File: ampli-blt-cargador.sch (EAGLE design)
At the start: 9 parts, among them IC1 TP4056

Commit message: correción de archivos
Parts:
- added BAT+, BAT+1, BAT-, BAT-1: LSP10, solpad:LSP10
- added C10, C7, C8, C9: 10uf, rcl:C-USC1206
- added C3, C4, C5, C6: (no value), rcl:C-EUC1206
- added IC2: TP4056, TP4056:TP4056
- added J1, J2, J3, J4: B2B-XH-A(LF)(SN), B2B-XH-A_LF__SN_:B2B-XH-A(LF)(SN)
- added J5, J6: UJC-HP-3-SMT-TR, UJC-HP-3-SMT-TR:UJC-HP-3-SMT-TR
- added LED3, LED4: (no value), led:LEDSML1206
- added R10, R11, R6, R7: 1k, rcl:R-US_R1206
- added R12, R8: 1k2, rcl:R-US_R1206
- added R5, R9: 0.4, rcl:R-US_R1206
- added U1: LM4950TSX/NOPB, LM4950TSX_NOPB:LM4950TSX/NOPB
- added XA1: B3P-VH(LF)(SN), B3P-VH_LF__SN_:B3P-VH(LF)(SN)
- C1, C2: device rcl:C-USC1206 -> rcl:C-EUC1206
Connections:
- new net N$10: C5.1, J2.2
- new net N$11: C2.2, J4.2
- new net N$13: C7.1, IC1.CE, IC1.VCC, LED1.A, LED2.A, R5.2
- new net N$14: LED1.C, R6.1
- new net N$15: IC1.CHRG, R6.2
- new net N$16: LED2.C, R7.1
- new net N$17: IC1.STDBY, R7.2
- new net N$18: IC1.PROG, R8.1
- new net N$19: C9.1, IC2.CE, IC2.VCC, LED3.A, LED4.A, R9.2
- new net N$20: LED3.C, R10.1
- new net N$21: IC2.CHRG, R10.2
- new net N$22: LED4.C, R11.1
- new net N$23: IC2.STDBY, R11.2
- new net N$24: IC2.PROG, R12.1
- new net N$7: C4.2, R4.2, U1.VOUTA
- new net N$8: C5.2, R3.2, U1.VOUTB
- new net N$9: C1.2, J3.2
- net GND: now also BAT-.MP, BAT-1.MP, C10.2, C3.2, C6.2, C7.2, C8.2, C9.2, IC2.GND, IC2.TEMP, J1.1, J2.1, J3.1, J4.1, J5.GND, J6.GND, R12.2, R8.2, U1.GND, U1.GND(TAB), U1.GND_2, XA1.1; no longer C1.2, C2.2, R4.2
- net N$1: now also R2.2, R3.1, U1.VINB; no longer C1.1, IC1.CE, IC1.VCC, LED1.A, LED2.A, R1.2
- net N$2: now also C2.1, R2.1; no longer IC1.PROG, R4.1
- net N$3: now also R1.2, R4.1, U1.VINA; no longer LED1.C, R2.1
- net N$4: now also C1.1, R1.1; no longer IC1.CHRG, R2.2
- net N$5: now also C6.1, U1.BYPASS; no longer LED2.C, R3.1
- net N$6: now also C4.1, J1.2; no longer IC1.STDBY, R3.2
- net VCC: now also J5.V-BUS, J6.V-BUS, R5.1, R9.1; no longer R1.1
- net VDD: now also BAT+.MP, BAT+1.MP, C10.1, C3.1, C8.1, IC2.BAT, U1.VDD, XA1.2, XA1.3; no longer C2.1
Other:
- note added: "amplificador"
- note added: "cargador"

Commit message: se termino el area de carga de pila, falta agregar el area de bluetooth
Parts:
- added C11: (no value), rcl:C-EUC1206
- added C12: 10uf, rcl:C-USC1206
- added IC3: DW01A, DW01A:DW01A
- added J7: B2B-XH-A(LF)(SN), B2B-XH-A_LF__SN_:B2B-XH-A(LF)(SN)
- added Q1: FS8205A, FS8205A:FS8205A
- added R13: 1k, rcl:R-US_R1206
- added R14: 100, rcl:R-US_R1206
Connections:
- new net B+: C10.1, C12.1, IC2.BAT, J7.2, R14.2
- new net B-: C10.2, C11.2, C12.2, IC3.GND, J7.1, Q1.S2
- new net N$12: IC3.CS, R13.1
- new net N$25: IC3.OC, Q1.G2
- new net N$26: IC3.OD, Q1.G1
- new net N$27: C11.1, IC3.VCC, R14.1
- net GND: now also Q1.S1, R13.2; no longer C10.2
- net VDD: no longer C10.1, IC2.BAT

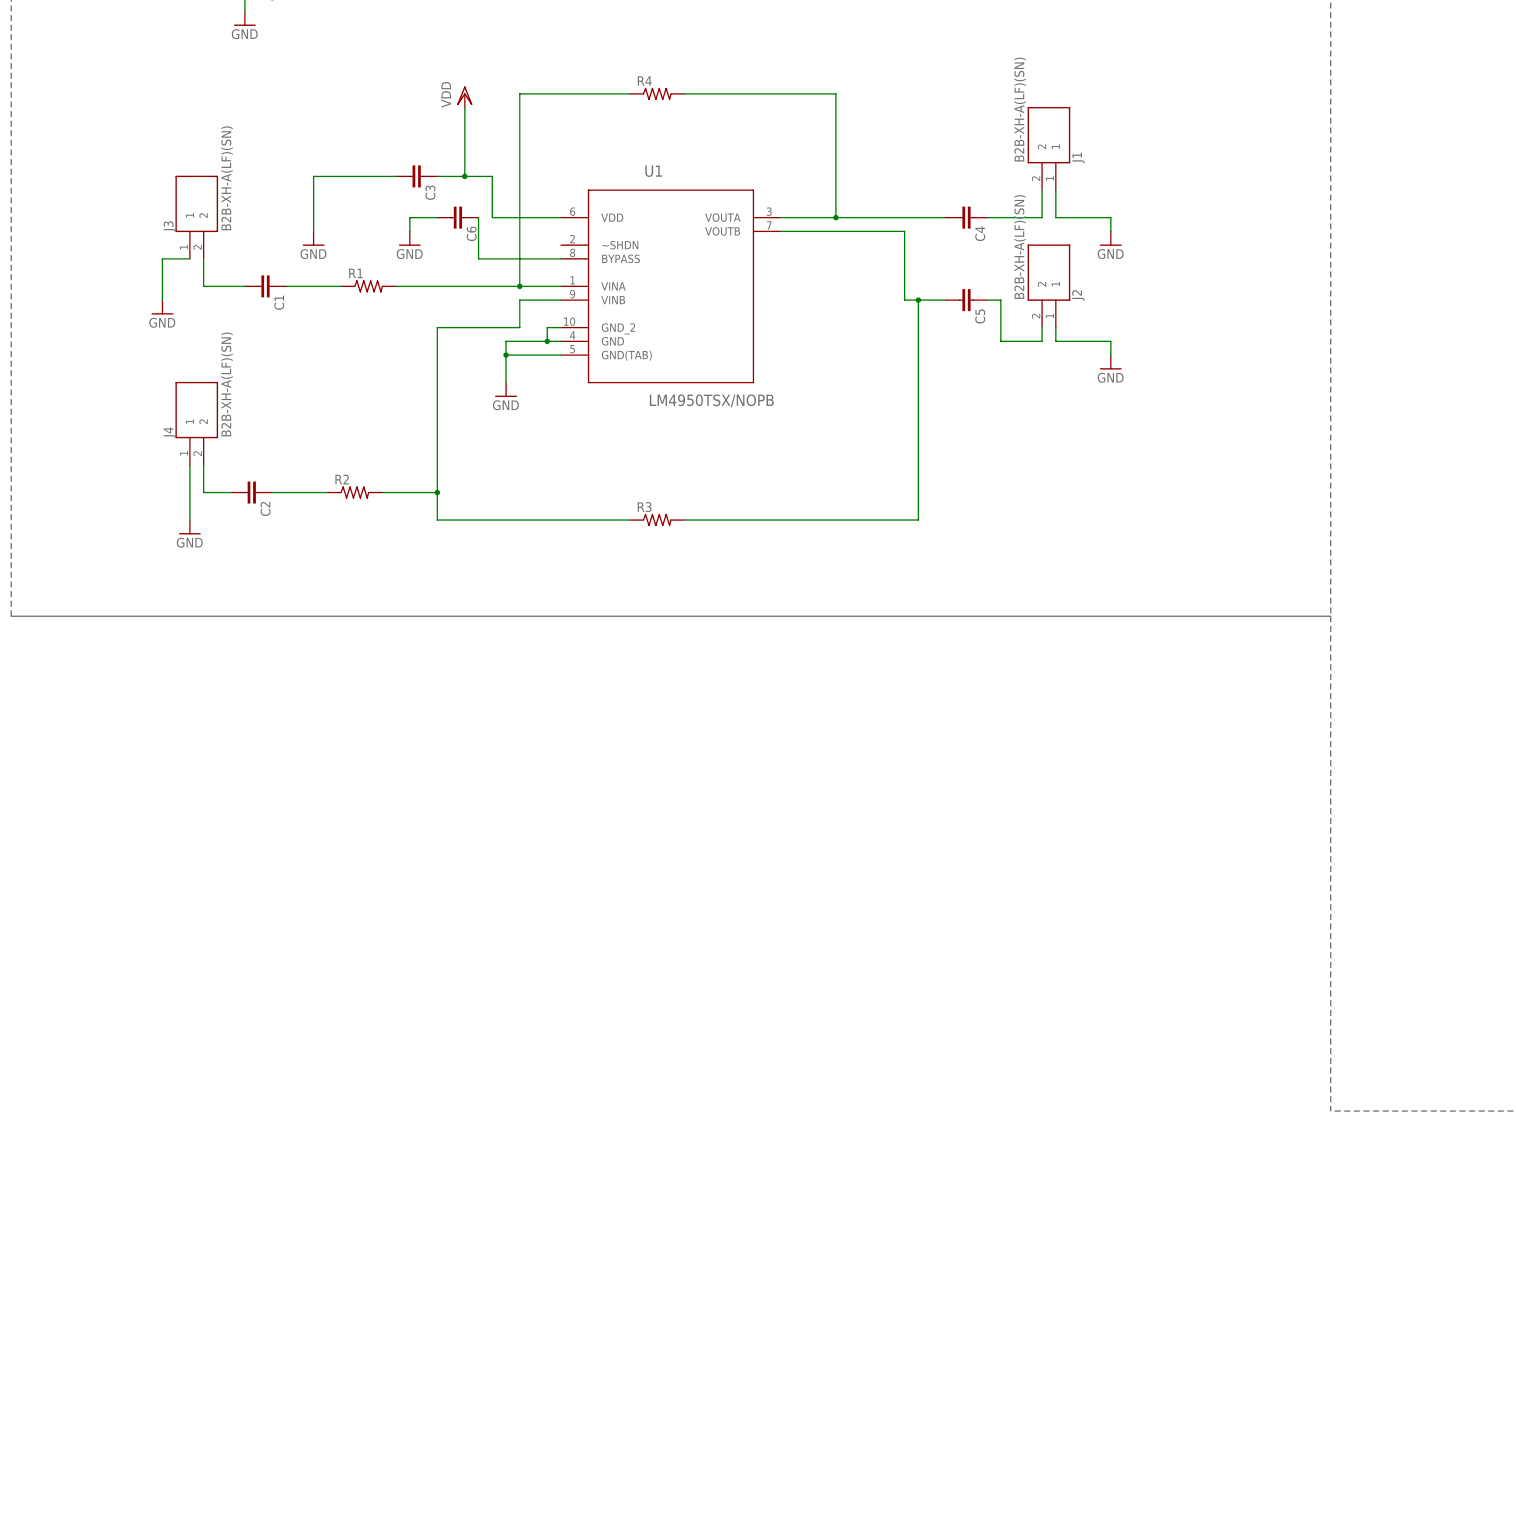
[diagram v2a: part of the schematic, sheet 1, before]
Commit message: se empezo a establecer las conexiones basicas del bluetooth
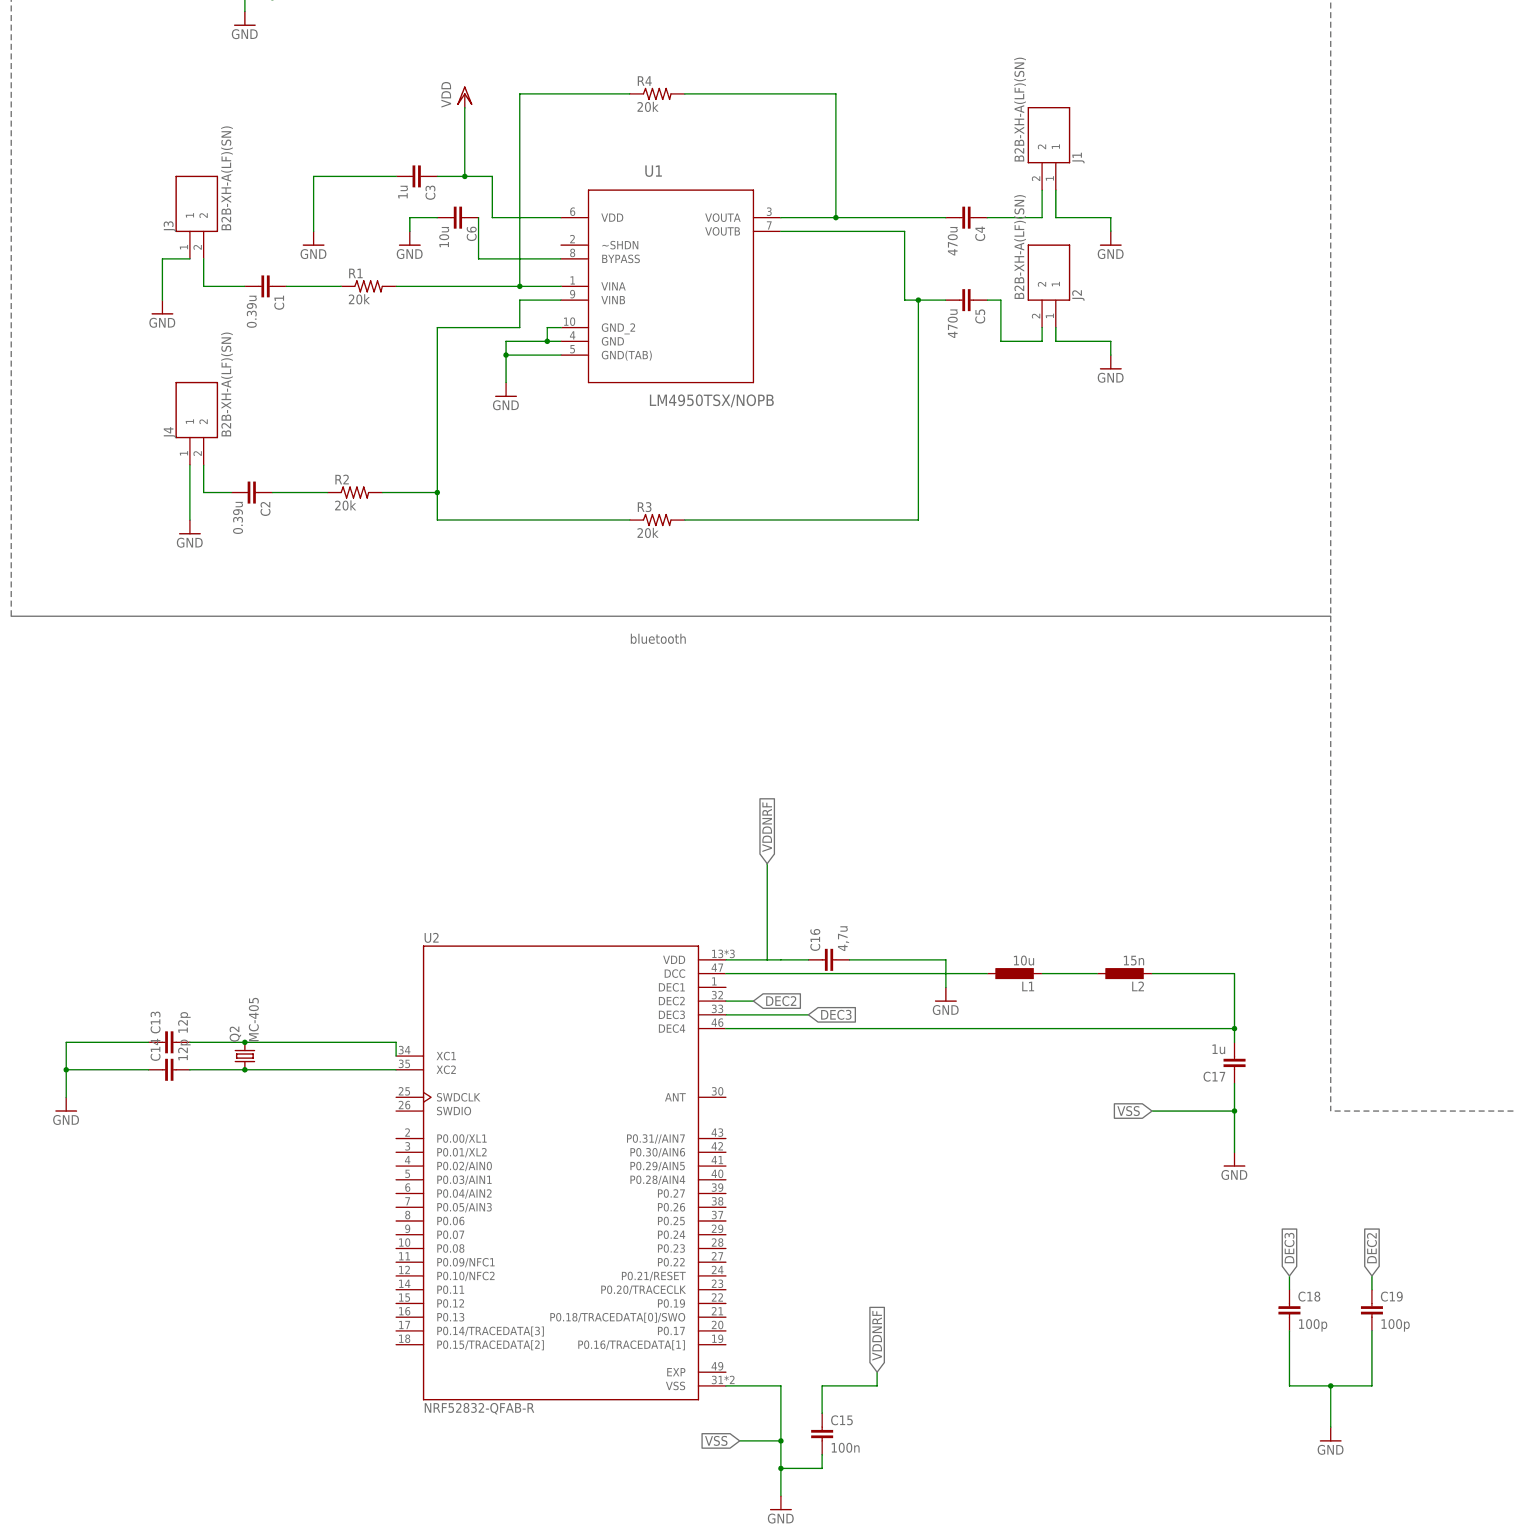
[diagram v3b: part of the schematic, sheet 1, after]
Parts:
- added C13, C14: 12p, rcl:C-EUC1206
- added C15: 100n, rcl:C-EUC1206
- added C16: 4,7u, rcl:C-EUC1206
- added C17: 1u, rcl:C-EUC1206
- added C18, C19: 100p, rcl:C-EUC1206
- added L1: 10u, rcl:L-EUL2012C
- added L2: 15n, rcl:L-EUL2012C
- added Q2: MC-405, crystal:MC-405
- added U2: NRF52832-QFAB-R, NRF52832-QFAB-R:NRF52832-QFAB-R
- C1, C2: value (none) -> 0.39u
- C3: value (none) -> 1u
- C4, C5: value (none) -> 470u
- C6: value (none) -> 10u
- R1, R2, R3, R4: value (none) -> 20k
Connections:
- new net DEC2: C19.1, U2.DEC2
- new net DEC3: C18.1, U2.DEC3
- new net N$28: C13.2, Q2.2, U2.XC1
- new net N$29: C14.2, Q2.1, U2.XC2
- new net N$30: L1.2, L2.1
- new net N$31: L1.1, U2.DCC
- new net N$32: C17.2, L2.2, U2.DEC4
- new net VDDNRF: C15.1, C16.1, U2.VDD
- new net VSS: C15.2, C17.1, U2.VSS
- net GND: now also C13.1, C14.1, C16.2, C18.2, C19.2
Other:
- note added: "bluetooth"
